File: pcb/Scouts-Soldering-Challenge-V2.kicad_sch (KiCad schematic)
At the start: 12 parts, among them J1 Barrel_Jack, SW1 SW_Push

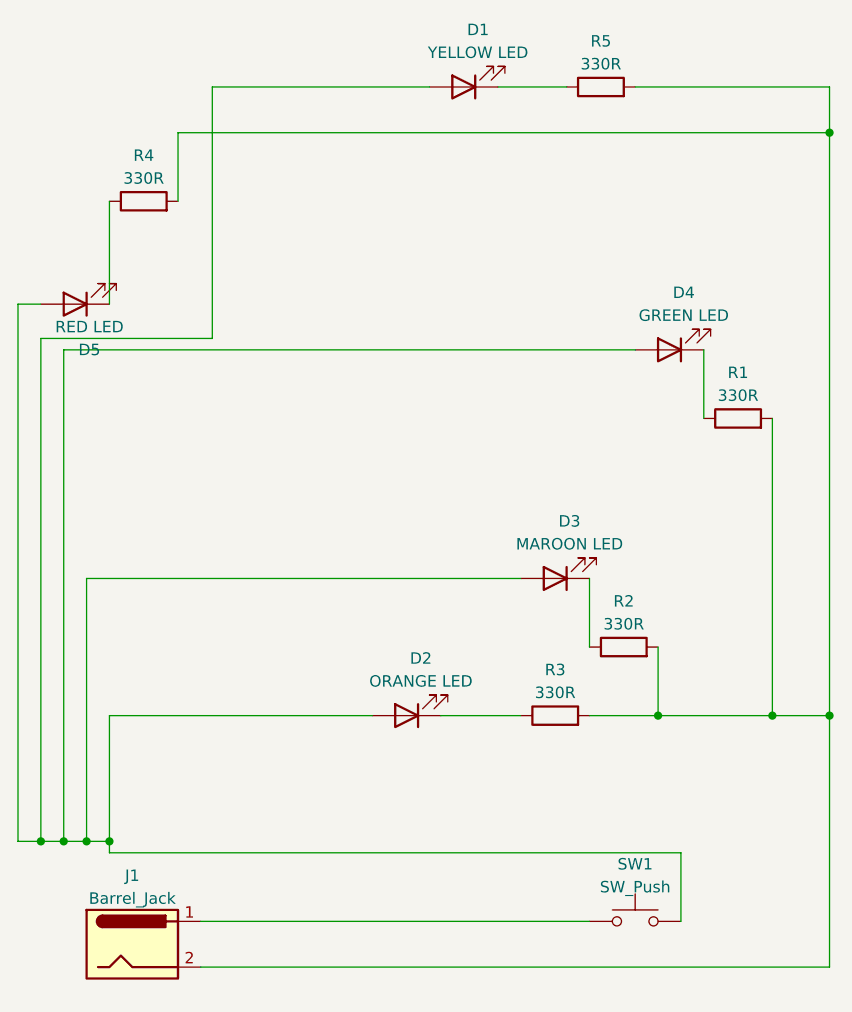
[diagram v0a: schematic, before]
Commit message: V2.1 of PCB and Schematic
Complete overhall, adds a buzzer, replaces the barrel jack with a battery and changes the resistors to match. Also moves things around a lot.
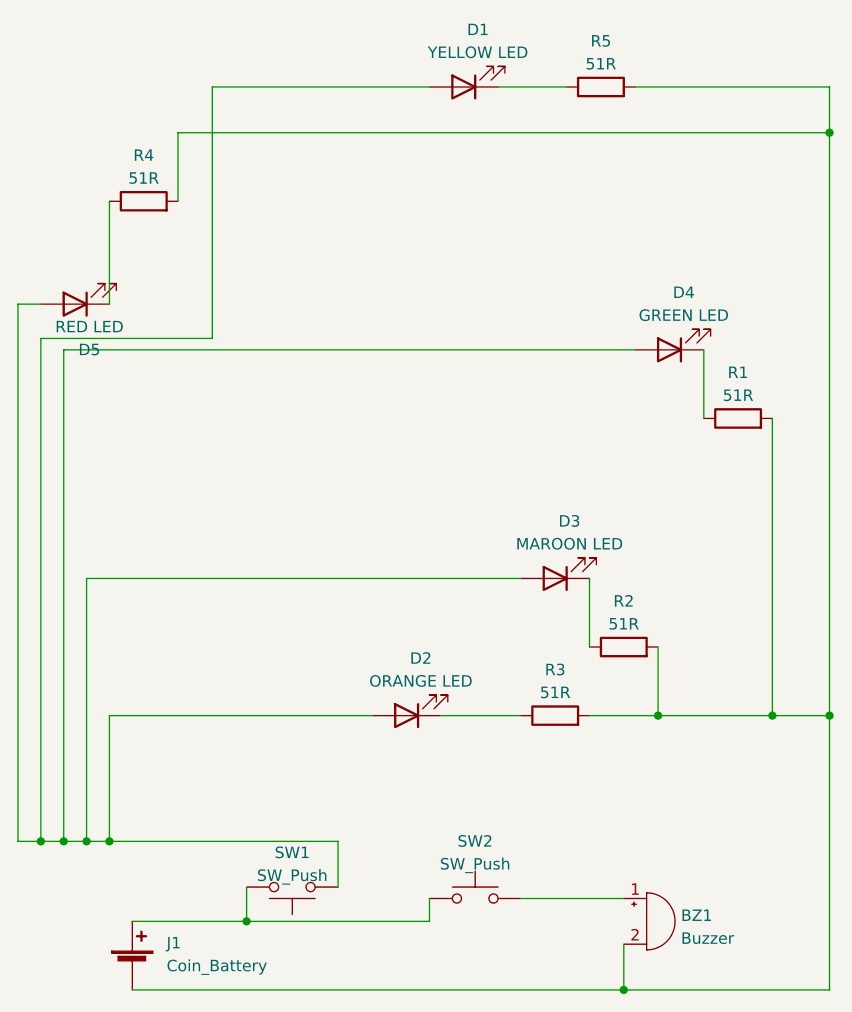
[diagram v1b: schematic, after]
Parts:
- added BZ1: Buzzer, Buzzer_Beeper:Buzzer_TDK_PS1240P02BT_D12.2mm_H6.5mm, symbol Device:Buzzer
- added SW2: SW_Push, Button_Switch_THT:SW_PUSH_6mm, symbol Switch:SW_Push
- J1: value Barrel_Jack -> Coin_Battery; footprint Connector_BarrelJack:BarrelJack_Horizontal -> Battery:BatteryHolder_Keystone_103_1x20mm; symbol Connector:Barrel_Jack -> Device:Battery_Cell
- R1, R2, R3, R4, R5: value 330R -> 51R
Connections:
- net at J1.2 (-), R1.2, R2.2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: now also BZ1.2 (+)
- net at D1.2 (A), D2.2 (A), D3.2 (A)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: now also SW1.1; no longer SW1.2
- net at J1.1 (+): now also SW1.2, SW2.1; no longer SW1.1
- new net: BZ1.1 (-), SW2.2
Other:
- moved on the sheet: SW1
